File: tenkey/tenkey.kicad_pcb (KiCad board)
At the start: 2 copper layers, 57.1 x 85.7 mm, 38 parts, among them SW0:0 NUM_0, SW0:2 DOT, SW1:0 NUM_1, SW1:1 NUM_2, SW1:2 NUM_3, SW1:3 ENTER, SW2:0 NUM_4, SW2:1 NUM_5, SW2:2 NUM_6, SW3:0 NUM_7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

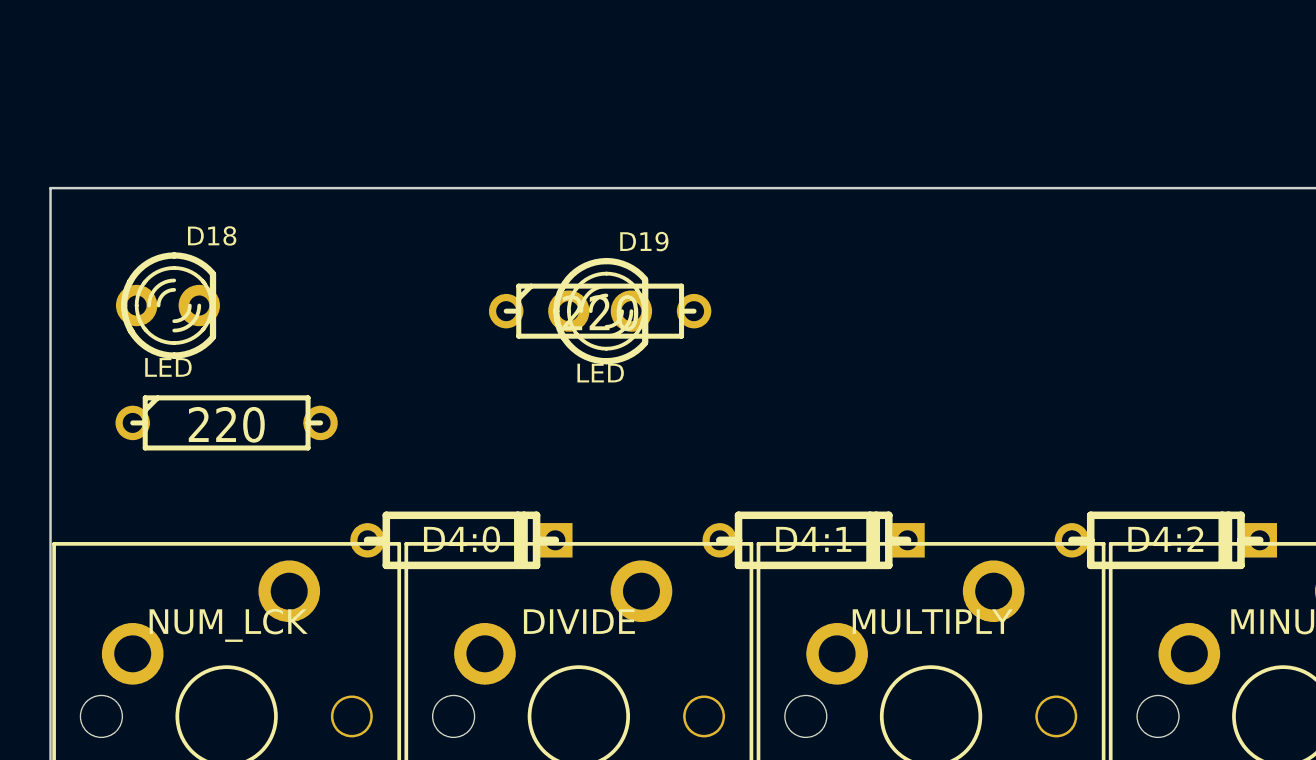
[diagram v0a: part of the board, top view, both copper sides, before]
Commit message: Fixed pinout on the Teensy2.0 module and updated the tenkey schematic/board
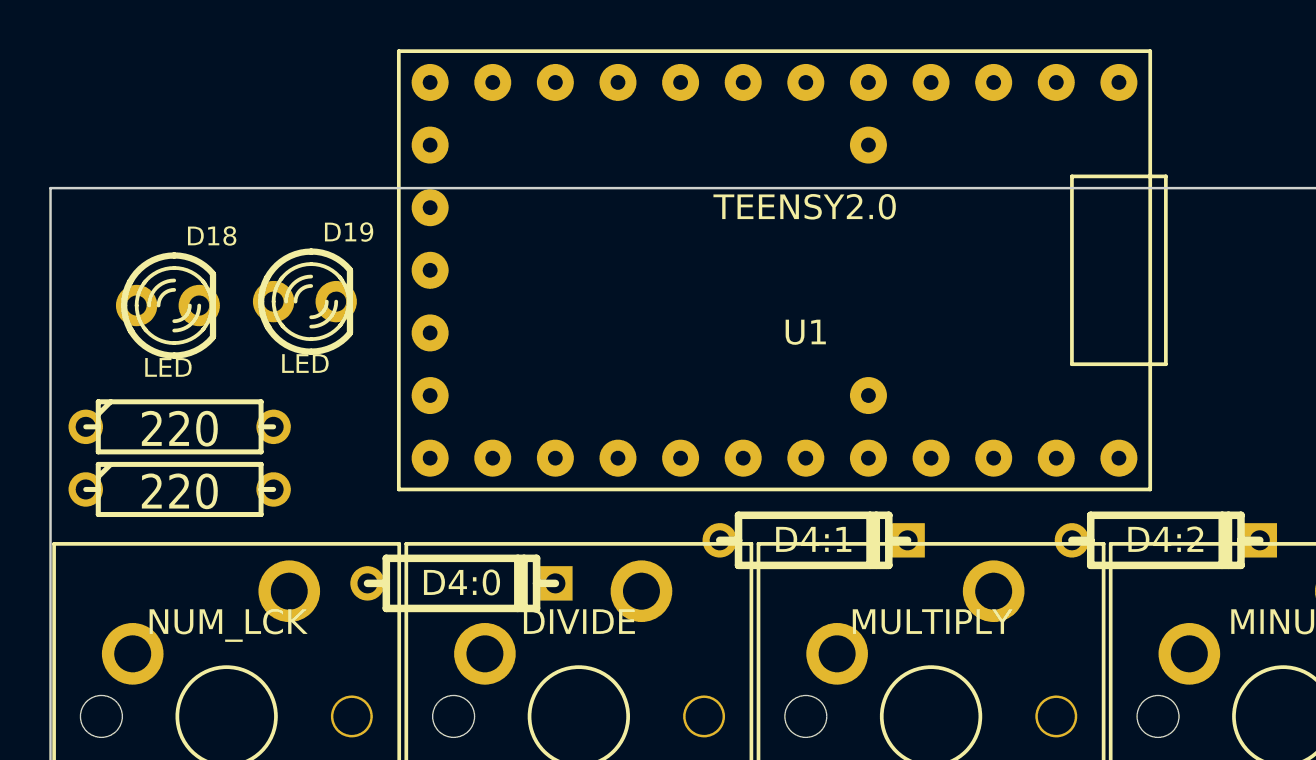
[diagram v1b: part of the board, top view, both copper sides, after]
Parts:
- added U1: TEENSY2.0, Keyboard:TEENSY2_0, F.Cu at (204.5, 53.3)
- moved R2 18.5 mm to (179.1, 62.2)
- moved D19 12.0 mm to (184.2, 54.6)
- moved R1 1.91 mm to (179.1, 59.7)
- moved D4:0 1.75 mm to (190.5, 66.0)
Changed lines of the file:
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@@
 (kicad_pcb (version 3) (host pcbnew "(2014-jan-25)-product")
   (general
-    (links 44)
-    (no_connects 44)
-    (area 0 0 0 0)
+    (links 56)
+    (no_connects 56)
+    (area 173.781249 49.956249 231.031251 135.781251)
     (thickness 1.6)
     (drawings 4)
     (tracks 0)
     (zones 0)
-    (modules 38)
-    (nets 33)
+    (modules 39)
+    (nets 52)
   )
   (page A4)
@@
   (net 31 /COL1)
   (net 32 /COL3)
+  (net 33 "Net-(U1-Pad4)")
+  (net 34 "Net-(U1-Pad5)")
+  (net 35 "Net-(U1-Pad6)")
+  (net 36 "Net-(U1-Pad7)")
+  (net 37 "Net-(U1-Pad23)")
+  (net 38 VCC)
+  (net 39 "Net-(U1-Pad16)")
+  (net 40 "Net-(U1-Pad20)")
+  (net 41 "Net-(U1-Pad21)")
+  (net 42 "Net-(U1-Pad24)")
+  (net 43 "Net-(U1-Pad8)")
+  (net 44 "Net-(U1-Pad10)")
+  (net 45 "Net-(U1-Pad17)")
+  (net 46 "Net-(U1-Pad18)")
+  (net 47 "Net-(U1-Pad19)")
+  (net 48 "Net-(U1-Pad29)")
+  (net 49 "Net-(U1-Pad26)")
+  (net 50 "Net-(U1-Pad30)")
+  (net 51 "Net-(U1-Pad25)")
   (net_class Default "This is the default net class."
     (clearance 0.254)
@@
     (add_net "Net-(R1-Pad2)")
     (add_net "Net-(R2-Pad1)")
+    (add_net "Net-(U1-Pad10)")
+    (add_net "Net-(U1-Pad16)")
+    (add_net "Net-(U1-Pad17)")
+    (add_net "Net-(U1-Pad18)")
+    (add_net "Net-(U1-Pad19)")
+    (add_net "Net-(U1-Pad20)")
+    (add_net "Net-(U1-Pad21)")
+    (add_net "Net-(U1-Pad23)")
+    (add_net "Net-(U1-Pad24)")
+    (add_net "Net-(U1-Pad25)")
+    (add_net "Net-(U1-Pad26)")
+    (add_net "Net-(U1-Pad29)")
+    (add_net "Net-(U1-Pad30)")
+    (add_net "Net-(U1-Pad4)")
+    (add_net "Net-(U1-Pad5)")
+    (add_net "Net-(U1-Pad6)")
+    (add_net "Net-(U1-Pad7)")
+    (add_net "Net-(U1-Pad8)")
+    (add_net VCC)
+  )
+  (module Keyboard:TEENSY2_0 (layer F.Cu)
+    (at 204.47 53.34 180)
+    (fp_text reference U1 (at 0 -2.54 180) (layer F.SilkS)
+      (effects (font (size 1 1) (thickness 0.15)))
+    )
+    (fp_text value TEENSY2.0 (at 0 2.54 180) (layer F.SilkS)
+      (effects (font (size 1 1) (thickness 0.15)))
+    )
+    (fp_line (start -14.605 -3.81) (end -14.605 3.81) (layer F.SilkS) (width 0.15))
+    (fp_line (start -14.605 3.81) (end -10.795 3.81) (layer F.SilkS) (width 0.15))
+    (fp_line (start -10.795 3.81) (end -10.795 -3.81) (layer F.SilkS) (width 0.15))
+    (fp_line (start -14.605 -3.81) (end -10.795 -3.81) (layer F.SilkS) (width 0.15))
+    (fp_line (start -13.97 -8.89) (end -13.97 8.89) (layer F.SilkS) (width 0.15))
+    (fp_line (start -13.97 8.89) (end 16.51 8.89) (layer F.SilkS) (width 0.15))
+    (fp_line (start 16.51 8.89) (end 16.51 -8.89) (layer F.SilkS) (width 0.15))
+    (fp_line (start 16.51 -8.89) (end -13.97 -8.89) (layer F.SilkS) (width 0.15))
+    (pad 0 thru_hole circle (at -10.16 7.62 180) (size 1.5 1.5) (drill 0.6) (layers *.Cu *.Mask F.SilkS)
+      (net 3 /ROW0))
+    (pad 1 thru_hole circle (at -7.62 7.62 180) (size 1.5 1.5) (drill 0.6) (layers *.Cu *.Mask F.SilkS)
+      (net 8 /ROW1))
+    (pad 2 thru_hole circle (at -5.08 7.62 180) (size 1.5 1.5) (drill 0.6) (layers *.Cu *.Mask F.SilkS)
+      (net 12 /ROW2))
+    (pad 3 thru_hole circle (at -2.54 7.62 180) (size 1.5 1.5) (drill 0.6) (layers *.Cu *.Mask F.SilkS)
+      (net 17 /ROW3))
+    (pad 4 thru_hole circle (at 0 7.62 180) (size 1.5 1.5) (drill 0.6) (layers *.Cu *.Mask F.SilkS)
+      (net 33 "Net-(U1-Pad4)"))
+    (pad 5 thru_hole circle (at 2.54 7.62 180) (size 1.5 1.5) (drill 0.6) (layers *.Cu *.Mask F.SilkS)
+      (net 34 "Net-(U1-Pad5)"))
+    (pad 6 thru_hole circle (at 5.08 7.62 180) (size 1.5 1.5) (drill 0.6) (layers *.Cu *.Mask F.SilkS)
+      (net 35 "Net-(U1-Pad6)"))
+    (pad 7 thru_hole circle (at 7.62 7.62 180) (size 1.5 1.5) (drill 0.6) (layers *.Cu *.Mask F.SilkS)
+      (net 36 "Net-(U1-Pad7)"))
+    (pad 8 thru_hole circle (at 10.16 7.62 180) (size 1.5 1.5) (drill 0.6) (layers *.Cu *.Mask F.SilkS)
+      (net 43 "Net-(U1-Pad8)"))
+    (pad 9 thru_hole circle (at 12.7 7.62 180) (size 1.5 1.5) (drill 0.6) (layers *.Cu *.Mask F.SilkS)
+      (net 22 /ROW4))
+    (pad 10 thru_hole circle (at 15.24 7.62 180) (size 1.5 1.5) (drill 0.6) (layers *.Cu *.Mask F.SilkS)
+      (net 44 "Net-(U1-Pad10)"))
+    (pad 23 thru_hole circle (at 15.24 5.08 180) (size 1.5 1.5) (drill 0.6) (layers *.Cu *.Mask F.SilkS)
+      (net 37 "Net-(U1-Pad23)"))
+    (pad 27 thru_hole circle (at 15.24 2.54 180) (size 1.5 1.5) (drill 0.6) (layers *.Cu *.Mask F.SilkS)
+      (net 38 VCC))
+    (pad 29 thru_hole circle (at 15.24 0 180) (size 1.5 1.5) (drill 0.6) (layers *.Cu *.Mask F.SilkS)
+      (net 48 "Net-(U1-Pad29)"))
+    (pad 26 thru_hole circle (at 15.24 -2.54 180) (size 1.5 1.5) (drill 0.6) (layers *.Cu *.Mask F.SilkS)
+      (net 49 "Net-(U1-Pad26)"))
+    (pad 22 thru_hole circle (at 15.24 -5.08 180) (size 1.5 1.5) (drill 0.6) (layers *.Cu *.Mask F.SilkS)
+      (net 29 /COL0))
+    (pad 11 thru_hole circle (at 15.24 -7.62 180) (size 1.5 1.5) (drill 0.6) (layers *.Cu *.Mask F.SilkS)
+      (net 31 /COL1))
+    (pad 12 thru_hole circle (at 12.7 -7.62 180) (size 1.5 1.5) (drill 0.6) (layers *.Cu *.Mask F.SilkS)
+      (net 30 /COL2))
+    (pad 13 thru_hole circle (at 10.16 -7.62 180) (size 1.5 1.5) (drill 0.6) (layers *.Cu *.Mask F.SilkS)
+      (net 32 /COL3))
+    (pad 14 thru_hole circle (at 7.62 -7.62 180) (size 1.5 1.5) (drill 0.6) (layers *.Cu *.Mask F.SilkS)
+      (net 23 /LED_A))
+    (pad 15 thru_hole circle (at 5.08 -7.62 180) (size 1.5 1.5) (drill 0.6) (layers *.Cu *.Mask F.SilkS)
+      (net 25 /LED_B))
+    (pad 16 thru_hole circle (at 2.54 -7.62 180) (size 1.5 1.5) (drill 0.6) (layers *.Cu *.Mask F.SilkS)
+      (net 39 "Net-(U1-Pad16)"))
+    (pad 17 thru_hole circle (at 0 -7.62 180) (size 1.5 1.5) (drill 0.6) (layers *.Cu *.Mask F.SilkS)
+      (net 45 "Net-(U1-Pad17)"))
+    (pad 18 thru_hole circle (at -2.54 -7.62 180) (size 1.5 1.5) (drill 0.6) (layers *.Cu *.Mask F.SilkS)
+      (net 46 "Net-(U1-Pad18)"))
+    (pad 19 thru_hole circle (at -5.08 -7.62 180) (size 1.5 1.5) (drill 0.6) (layers *.Cu *.Mask F.SilkS)
+      (net 47 "Net-(U1-Pad19)"))
+    (pad 20 thru_hole circle (at -7.62 -7.62 180) (size 1.5 1.5) (drill 0.6) (layers *.Cu *.Mask F.SilkS)
+      (net 40 "Net-(U1-Pad20)"))
+    (pad 21 thru_hole circle (at -10.16 -7.62 180) (size 1.5 1.5) (drill 0.6) (layers *.Cu *.Mask F.SilkS)
+      (net 41 "Net-(U1-Pad21)"))
+    (pad 28 thru_hole circle (at -12.7 -7.62 180) (size 1.5 1.5) (drill 0.6) (layers *.Cu *.Mask F.SilkS)
+      (net 38 VCC))
+    (pad 30 thru_hole circle (at -12.7 7.62 180) (size 1.5 1.5) (drill 0.6) (layers *.Cu *.Mask F.SilkS)
+      (net 50 "Net-(U1-Pad30)"))
+    (pad 25 thru_hole circle (at -2.54 -5.08 180) (size 1.5 1.5) (drill 0.6) (layers *.Cu *.Mask F.SilkS)
+      (net 51 "Net-(U1-Pad25)"))
+    (pad 24 thru_hole circle (at -2.54 5.08 180) (size 1.5 1.5) (drill 0.6) (layers *.Cu *.Mask F.SilkS)
+      (net 42 "Net-(U1-Pad24)"))
   )
   (module Discret:D3 (layer F.Cu)
@@
   )
   (module Discret:D3 (layer F.Cu)
-    (at 190.5 64.29375)
+    (at 190.5 66.04)
     (descr "Diode 3 pas")
     (tags "DIODE DEV")
@@
   )
   (module LEDs:LED-3MM (layer F.Cu)
-    (at 196.1261 54.99735)
+    (at 184.15 54.61)
     (descr "LED 3mm - Lead pitch 100mil (2,54mm)")
     (tags "LED led 3mm 3MM 100mil 2,54mm")
@@
   )
   (module Discret:R3 (layer F.Cu)
-    (at 180.975 59.53125)
+    (at 179.07 59.69)
     (descr "Resitance 3 pas")
     (tags R)
@@
   )
   (module Discret:R3 (layer F.Cu)
-    (at 196.1261 54.99735)
+    (at 179.07 62.23)
     (descr "Resitance 3 pas")
     (tags R)

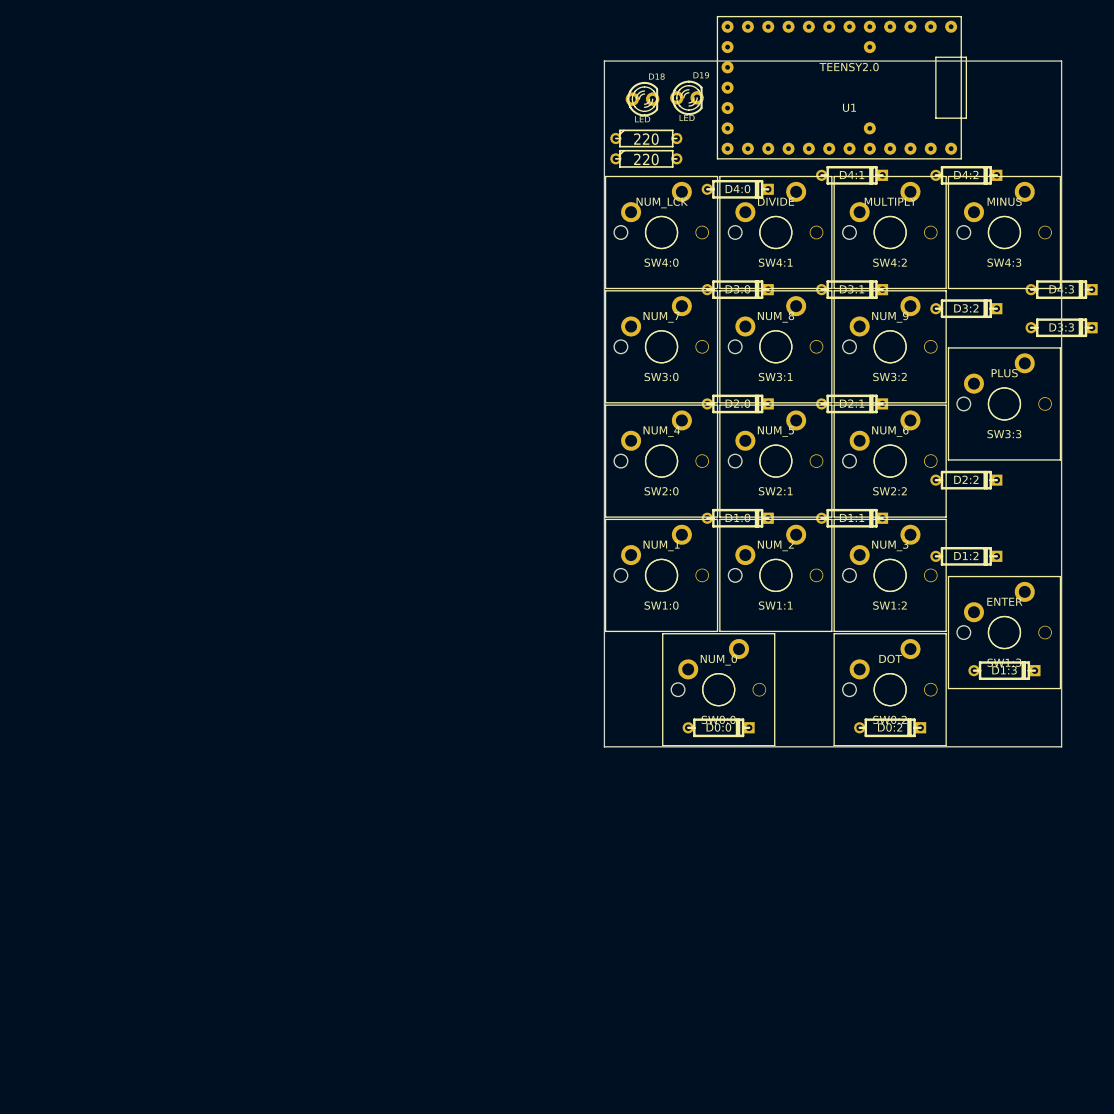
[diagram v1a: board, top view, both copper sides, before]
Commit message: apparently, you need some space between the keyswitches to make room for the caps
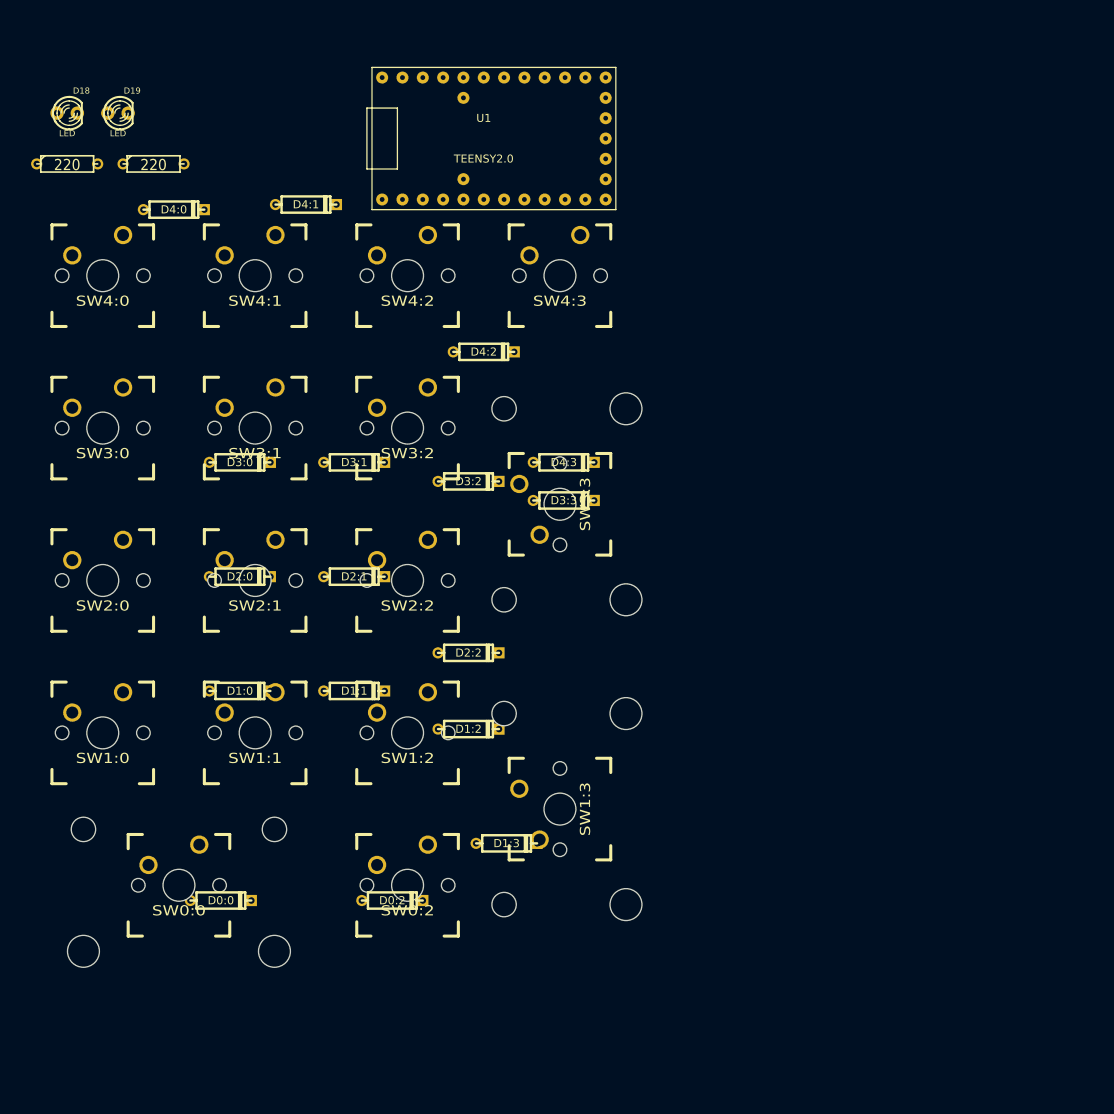
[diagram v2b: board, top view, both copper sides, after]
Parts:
- SW0:0: footprint Keyboard:KEYMODULE_MX_PINS -> Keyboard:CHERRY_PCB_200H
- SW0:2, SW1:0, SW1:1, SW1:2, SW2:0, SW2:1, SW2:2, SW3:0, SW3:1, SW3:2, SW4:0, SW4:1, SW4:2, SW4:3: footprint Keyboard:KEYMODULE_MX_PINS -> 1u:CHERRY_PCB_100H
- SW1:3, SW3:3: footprint Keyboard:KEYMODULE_MX_PINS -> Keyboard:CHERRY_PCB_200V
- moved SW1:0 72.6 mm to (111.1, 134.0)
- moved R1 72.5 mm to (106.7, 62.9)
- moved D18 71.9 mm to (106.7, 56.5)
- moved SW0:0 71.8 mm to (120.7, 153.0)
- moved SW2:0 71.4 mm to (111.1, 114.9)
- moved D19 71.1 mm to (113.0, 56.5)
- moved SW3:0 70.6 mm to (111.1, 95.9)
- moved D4:0 70.5 mm to (120.0, 68.6)
- moved SW4:0 70.1 mm to (111.1, 76.8)
- moved D4:1 68.4 mm to (136.5, 67.9)
- moved SW1:1 68.0 mm to (130.2, 134.0)
- moved SW2:1 66.8 mm to (130.2, 114.9)
- moved SW3:1 65.9 mm to (130.2, 95.9)
- moved D0:2 65.9 mm to (147.3, 154.9)
- moved D0:0 65.9 mm to (125.9, 154.9)
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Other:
- board outline removed

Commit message: fixed the vertical 2 unit switch footprint and routed some tenkey
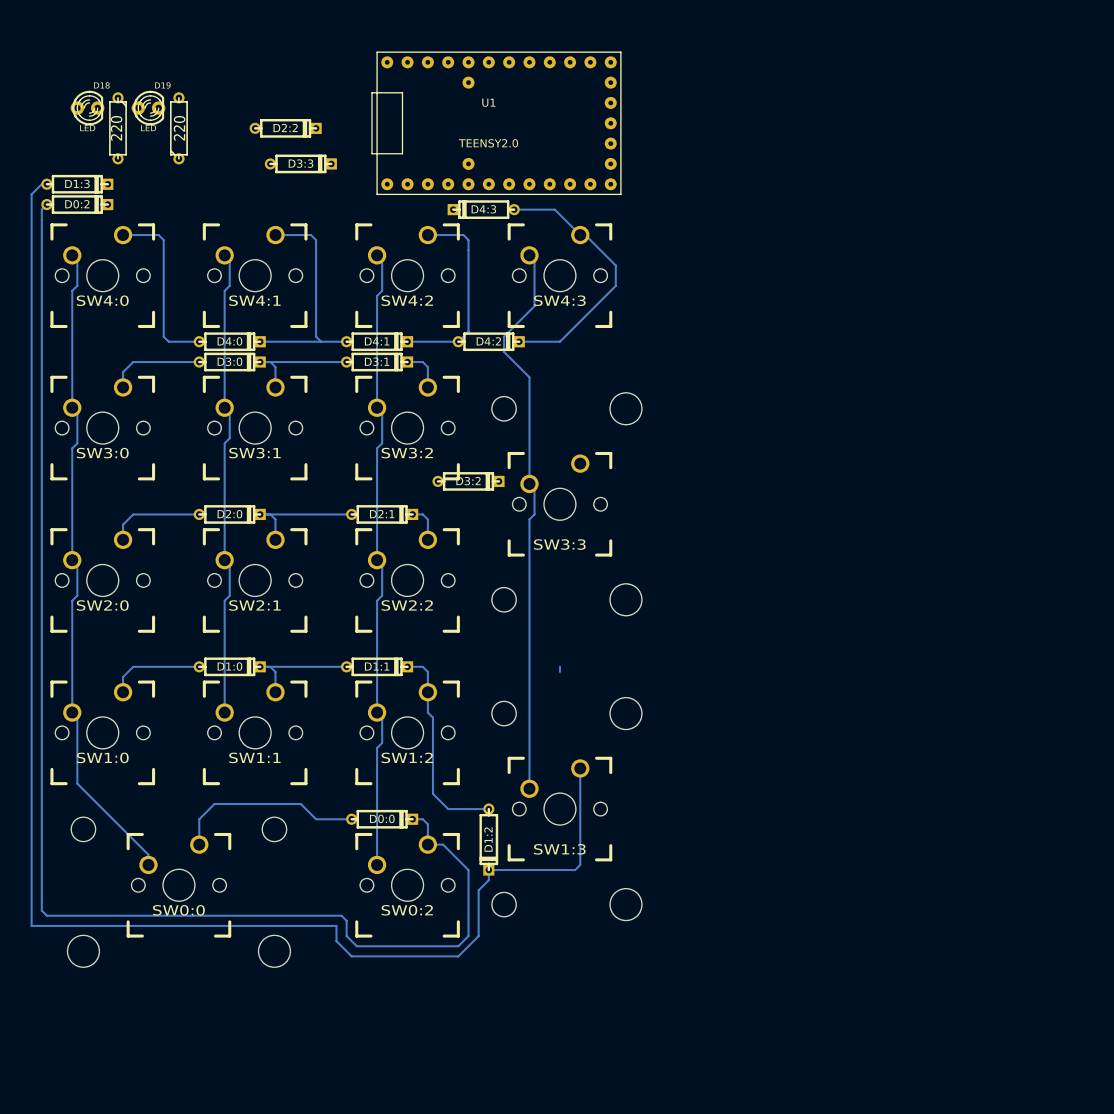
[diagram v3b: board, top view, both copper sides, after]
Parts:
- moved D1:3 98.3 mm to (108.0, 65.4)
- moved D0:2 95.5 mm to (108.0, 67.9)
- moved D2:2 69.4 mm to (134.0, 58.4)
- moved D3:3 53.4 mm to (135.9, 62.9)
- moved D4:3 33.1 mm to (158.8, 68.6), turned to 180 degrees
- moved D0:0 22.6 mm to (146.1, 144.8)
- moved D4:1 19.3 mm to (145.4, 85.1)
- moved D4:0 17.9 mm to (127.0, 85.1)
- moved D1:2 14.0 mm to (159.4, 147.3), turned to 270 degrees
- moved D3:1 12.9 mm to (145.4, 87.6)
- moved D3:0 12.6 mm to (127.0, 87.6)
- moved D2:1 8.53 mm to (146.1, 106.7)
- moved D2:0 7.88 mm to (127.0, 106.7)
- moved R1 7.75 mm to (113.0, 58.4), turned to 270 degrees
- moved R2 5.46 mm to (120.7, 58.4), turned to 90 degrees
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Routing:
- net Net-(D1:2-Pad2): track 0.00 -> 186.0 mm
- net Net-(D0:0-Pad2): track 0.00 -> 164.7 mm
- net /COL0: track 0.00 -> 81.7 mm
- net /COL2: track 0.00 -> 78.3 mm
- net /COL3: track 0.00 -> 71.3 mm
- net /COL1: track 0.00 -> 58.7 mm
- net Net-(D4:2-Pad2): track 0.00 -> 33.1 mm
- net Net-(D4:0-Pad2): track 0.00 -> 29.1 mm
- net Net-(D1:1-Pad2): track 0.00 -> 26.1 mm
- net Net-(D4:1-Pad2): track 0.00 -> 24.9 mm
- net Net-(D0:0-Pad1): track 0.00 -> 23.8 mm
- net Net-(D4:0-Pad1): track 0.00 -> 22.1 mm
- net Net-(D2:0-Pad2): track 0.00 -> 16.1 mm
- net Net-(D3:0-Pad2): track 0.00 -> 15.5 mm
- net Net-(D1:0-Pad2): track 0.00 -> 15.5 mm
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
